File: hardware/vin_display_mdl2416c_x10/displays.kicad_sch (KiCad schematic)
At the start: 10 parts, among them U10 MDL2416C, U11 MDL2416C, U12 MDL2416C, U13 MDL2416C, U14 MDL2416C, U5 MDL2416C, U6 MDL2416C, U7 MDL2416C, U8 MDL2416C, U9 MDL2416C

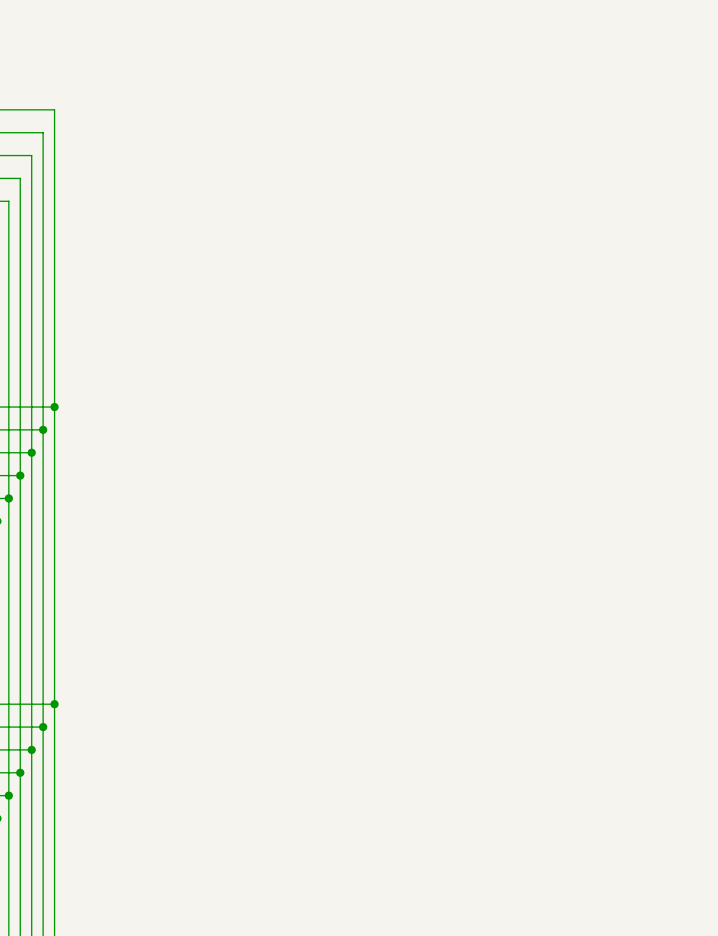
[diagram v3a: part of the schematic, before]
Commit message: minor pcb changes; add decoupling caps in mdl2416c_x10
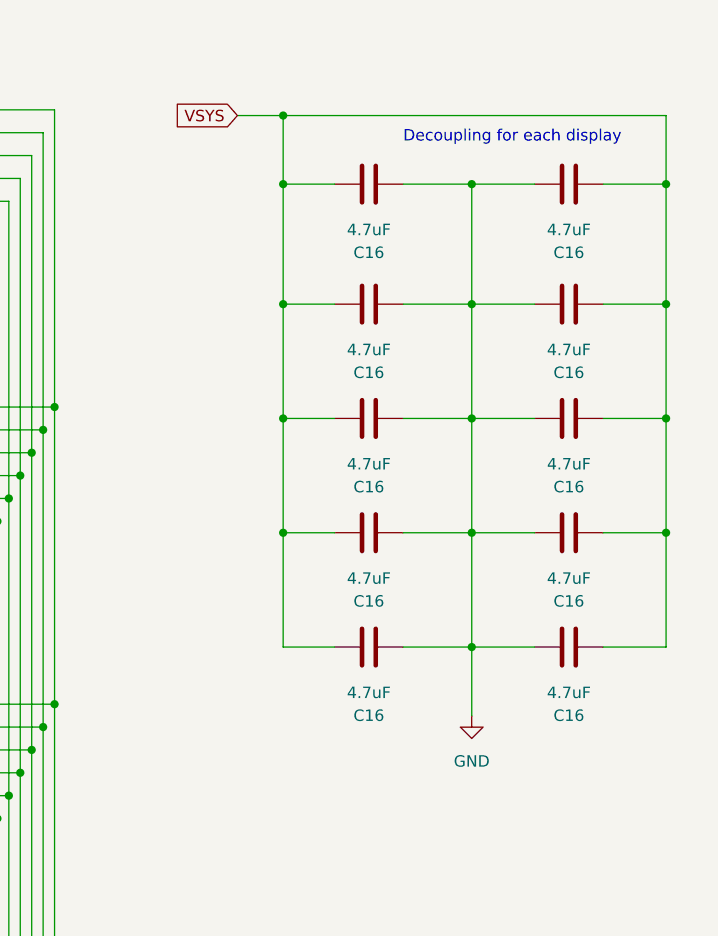
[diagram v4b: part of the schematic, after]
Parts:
- added C16 (x10): 4.7uF, Capacitor_SMD:C_0805_2012Metric, symbol Device:C
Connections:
- net GND: now also C16.1, C16.1, C16.1, C16.1, C16.1, C16.2, C16.2, C16.2, C16.2, C16.2
- net VSYS: now also C16.1, C16.1, C16.1, C16.1, C16.1, C16.2, C16.2, C16.2, C16.2, C16.2
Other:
- note added: "Decoupling for each display"
